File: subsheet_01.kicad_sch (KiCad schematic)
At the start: 0 parts

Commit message: Begins the CPU
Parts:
- added NT1: NetTie_2, symbol Device:NetTie_2
- added U1: MC68000_PLCC_68_PHY, Package_LCC:PLCC-68_THT-Socket, symbol mc_68000_plcc68:MC68000_PLCC_68_PHY
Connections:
- new net A1: U1.32 (A1)
- new net A10: U1.41 (A10)
- new net A11: U1.42 (A11)
- new net A12: U1.43 (A12)
- new net A13: U1.44 (A13)
- new net A14: U1.45 (A14)
- new net A15: U1.46 (A15)
- new net A16: U1.47 (A16)
- new net A17: U1.48 (A17)
- new net A18: U1.49 (A18)
- new net A19: U1.50 (A19)
- new net A2: U1.33 (A2)
- new net A20: U1.51 (A20)
- new net A21: U1.53 (A21)
- new net A22: U1.54 (A22)
- new net A23: U1.55 (A23)
- new net A3: U1.34 (A3)
- new net A4: U1.35 (A4)
- new net A5: U1.36 (A5)
- new net A6: U1.37 (A6)
- new net A7: U1.38 (A7)
- new net A8: U1.39 (A8)
- new net A9: U1.40 (A9)
- new net CPU_CLOCK: U1.15 (CLK)
- new net CPU_R/~{W}: U1.9 (R/~{W})
- new net D0: U1.5 (D0)
- new net D1: U1.4 (D1)
- new net D10: U1.63 (D10)
- new net D11: U1.62 (D11)
- new net D12: U1.61 (D12)
- new net D13: U1.60 (D13)
- new net D14: U1.59 (D14)
- new net D15: U1.58 (D15)
- new net D2: U1.3 (D2)
- new net D3: U1.2 (D3)
- new net D4: U1.1 (D4)
- new net D5: U1.68 (D5)
- new net D6: U1.67 (D6)
- new net D7: U1.66 (D7)
- new net D8: U1.65 (D8)
- new net D9: U1.64 (D9)
- new net FC0: U1.30 (FC0)
- new net FC1: U1.29 (FC1)
- new net FC2: U1.28 (FC2)
- new net IPL0: U1.27 (IPL0)
- new net IPL1: U1.26 (IPL1)
- new net IPL2: U1.25 (IPL2)
- new net ~{CPU_AS}: U1.6 (~{AS})
- new net ~{CPU_BGACK}: U1.12 (~{BGACK})
- new net ~{CPU_BG}: U1.11 (~{BG})
- new net ~{CPU_BR}: U1.13 (~{BR})
- new net ~{CPU_DTACK}: U1.10 (~{DTACK})
- new net ~{CPU_HALT}: U1.19 (~{HALT})
- new net ~{CPU_LDS}: U1.8 (~{LDS})
- new net ~{CPU_RESET}: U1.20 (~{RESET})
- new net ~{CPU_UDS}: U1.7 (~{UDS})
- no-connect marks 0 -> 3

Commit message: Continue CPU
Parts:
- added C1, C2: 0.22uF, symbol Device:C_Small
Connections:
- net 3V3_CPU: now reaches U1.14 (VCC)
- net 3V3_CPU: now also NT1.2, U1.52 (VCC), C1.1, C2.1
- net GND: now reaches U1.16 (GND)
- net GND: now also U1.17 (GND), U1.56 (GND), U1.57 (GND), C1.2, C2.2
- net +3V3: now reaches NT1.1
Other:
- note added: "TODO : * pull-up (give local labels to signals) * A0, A[24..31] and D[16..31] are left alone * ~{BERR} is missing !"
- moved on the sheet: NT1

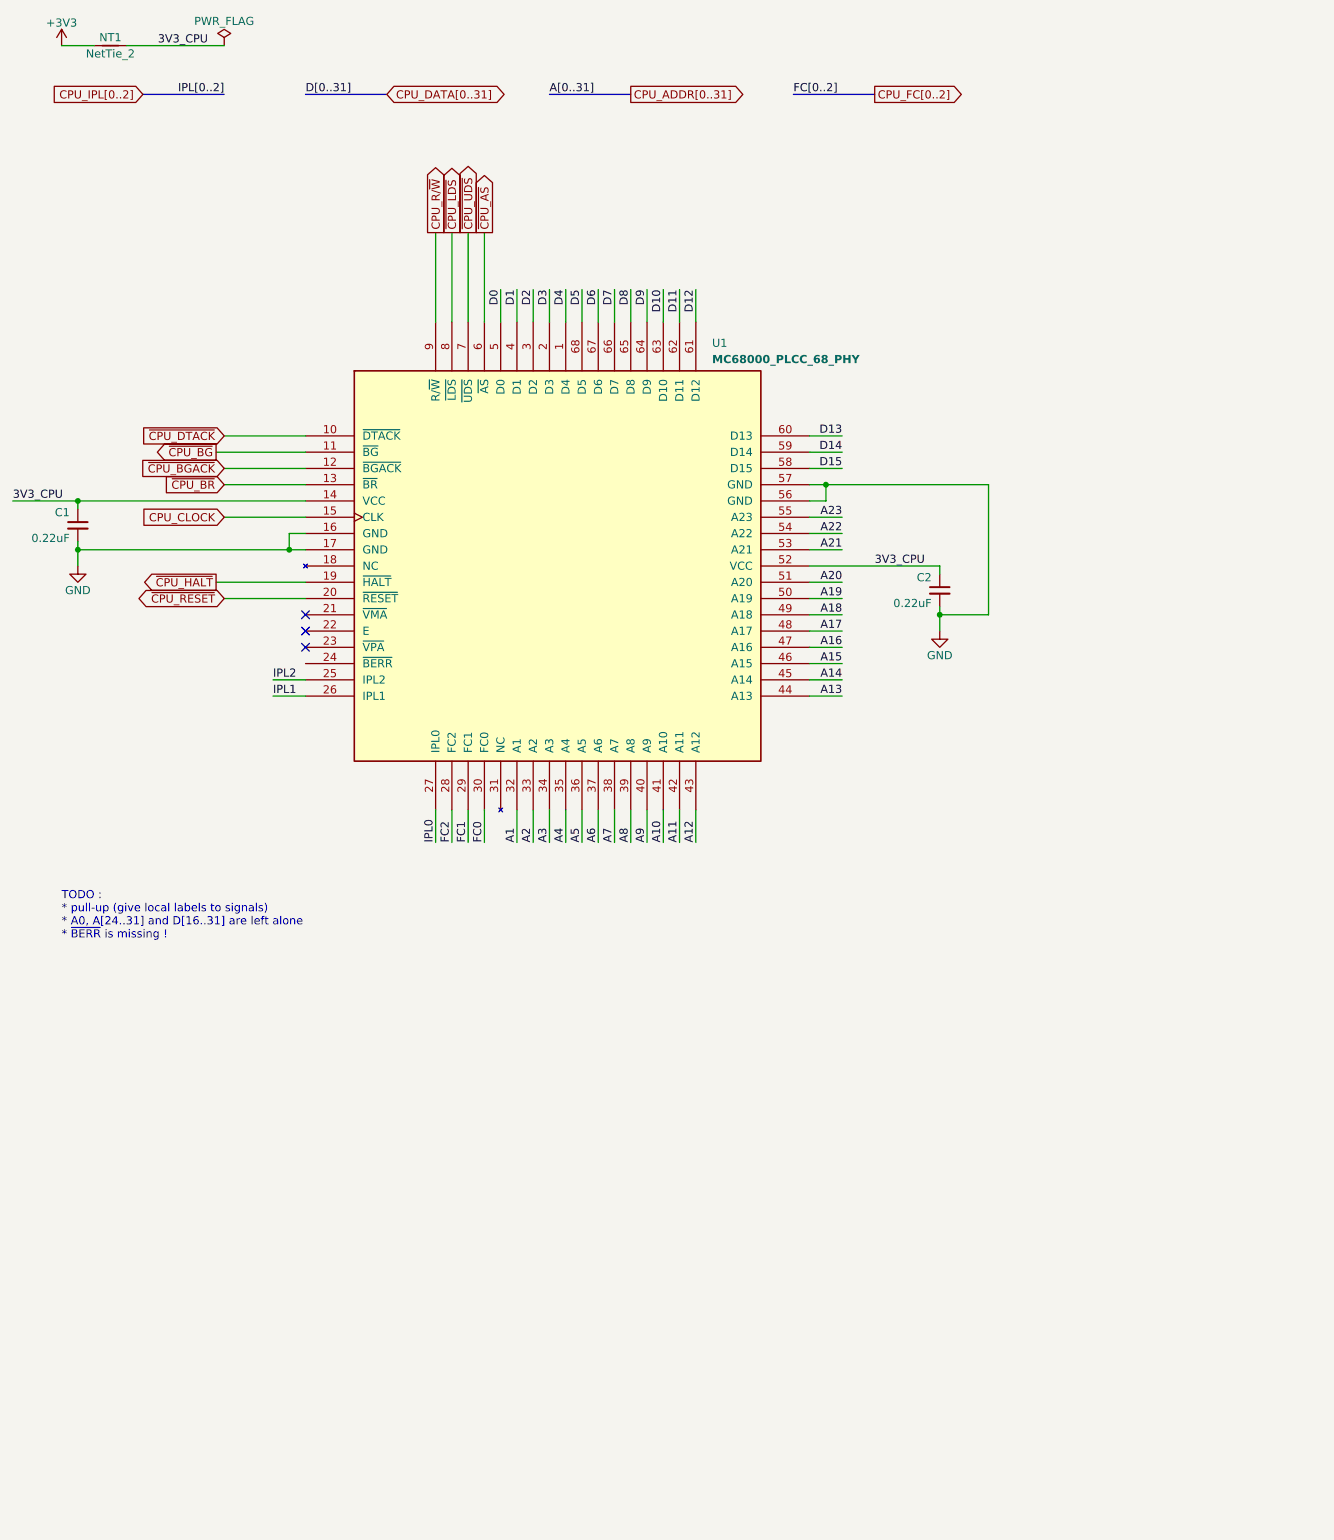
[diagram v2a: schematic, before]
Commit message: Completed CPU (for now), added notes to power supply sheet
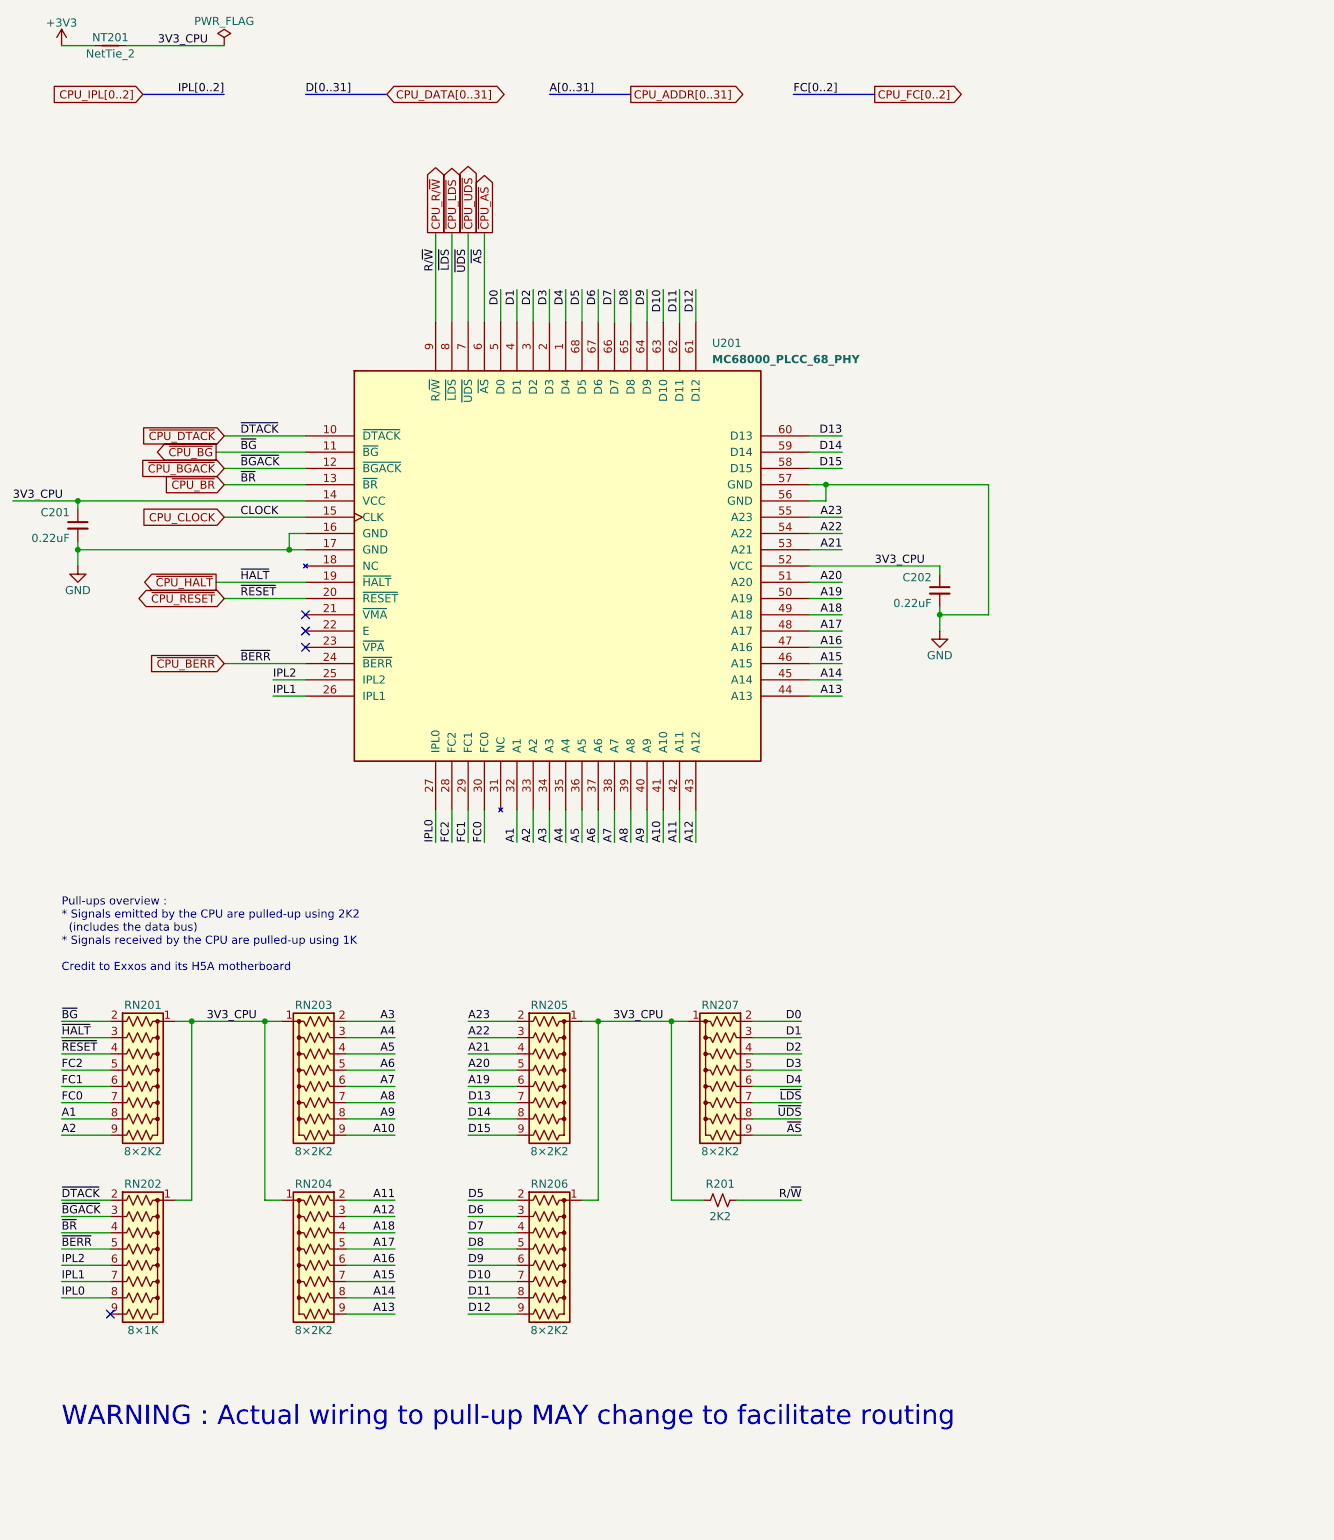
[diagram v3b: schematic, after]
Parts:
- added R201: 2K2, symbol Device:R_Small_US
- added RN201, RN203, RN204, RN205, RN206, RN207: 8×2K2, Resistor_THT:R_Array_SIP9, symbol Device:R_Network08_US
- added RN202: 8×1K, Resistor_THT:R_Array_SIP9, symbol Device:R_Network08_US
- renumbered C1 to C201, C2 to C202, NT1 to NT201, U1 to U201
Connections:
- net 3V3_CPU: now also R201.1, RN201.1 (common), RN202.1 (common), RN203.1 (common), RN204.1 (common), RN205.1 (common), RN206.1 (common), RN207.1 (common)
- net A1: now also RN201.8 (R7)
- net A10: now also RN203.9 (R8)
- net A11: now also RN204.2 (R1)
- net A12: now also RN204.3 (R2)
- net A13: now also RN204.9 (R8)
- net A14: now also RN204.8 (R7)
- net A15: now also RN204.7 (R6)
- net A16: now also RN204.6 (R5)
- net A17: now also RN204.5 (R4)
- net A18: now also RN204.4 (R3)
- net A19: now also RN205.6 (R5)
- net A2: now also RN201.9 (R8)
- net A20: now also RN205.5 (R4)
- net A21: now also RN205.4 (R3)
- net A22: now also RN205.3 (R2)
- net A23: now also RN205.2 (R1)
- net A3: now also RN203.2 (R1)
- net A4: now also RN203.3 (R2)
- net A5: now also RN203.4 (R3)
- net A6: now also RN203.5 (R4)
- net A7: now also RN203.6 (R5)
- net A8: now also RN203.7 (R6)
- net A9: now also RN203.8 (R7)
- net CPU_R/~{W}: now also R201.2
- net D0: now also RN207.2 (R1)
- net D1: now also RN207.3 (R2)
- net D10: now also RN206.7 (R6)
- net D11: now also RN206.8 (R7)
- net D12: now also RN206.9 (R8)
- net D13: now also RN205.7 (R6)
- net D14: now also RN205.8 (R7)
- net D15: now also RN205.9 (R8)
- net D2: now also RN207.4 (R3)
- net D3: now also RN207.5 (R4)
- net D4: now also RN207.6 (R5)
- net D5: now also RN206.2 (R1)
- net D6: now also RN206.3 (R2)
- net D7: now also RN206.4 (R3)
- net D8: now also RN206.5 (R4)
- net D9: now also RN206.6 (R5)
- net FC0: now also RN201.7 (R6)
- net FC1: now also RN201.6 (R5)
- net FC2: now also RN201.5 (R4)
- net IPL0: now also RN202.8 (R7)
- net IPL1: now also RN202.7 (R6)
- net IPL2: now also RN202.6 (R5)
- net ~{CPU_AS}: now also RN207.9 (R8)
- net ~{CPU_BGACK}: now also RN202.3 (R2)
- net ~{CPU_BG}: now also RN201.2 (R1)
- net ~{CPU_BR}: now also RN202.4 (R3)
- net ~{CPU_DTACK}: now also RN202.2 (R1)
- net ~{CPU_HALT}: now also RN201.3 (R2)
- net ~{CPU_LDS}: now also RN207.7 (R6)
- net ~{CPU_RESET}: now also RN201.4 (R3)
- net ~{CPU_UDS}: now also RN207.8 (R7)
- net ~{CPU_BERR}: now reaches U201.24 (~{BERR})
- net ~{CPU_BERR}: now also RN202.5 (R4)
- no-connect marks 3 -> 4
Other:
- note added: "Pull-ups overview : * Signals emitted by the CPU are pulled-up using 2K2 (includes the data bus) * Signals received by the CPU are pulled-up using 1K Credit to Exxos and its H5A motherboard"
- note added: "WARNING : Actual wiring to pull-up MAY change to facilitate routing"
- note removed: "TODO : * pull-up (give local labels to signals) * A0, A[24..31] and D[16..31] are left alone * ~{BERR} is missing !"

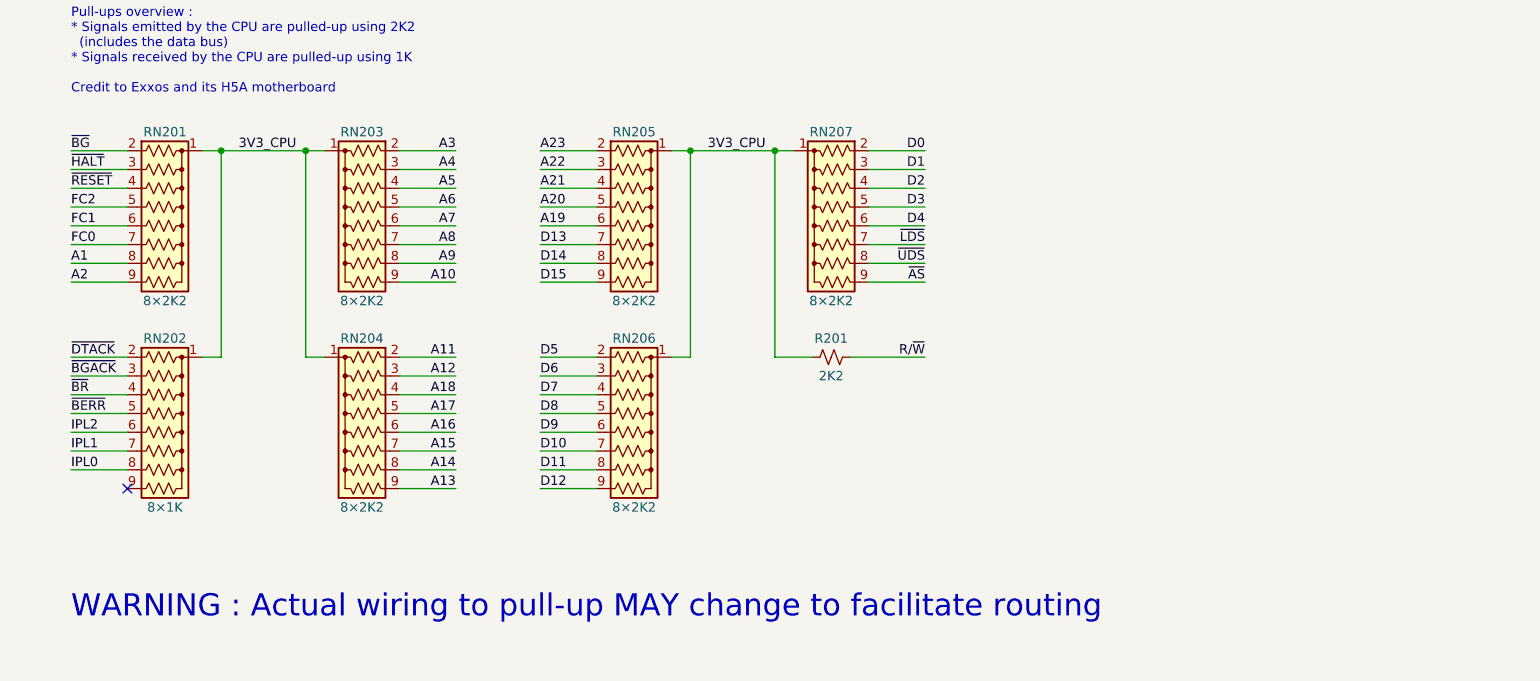
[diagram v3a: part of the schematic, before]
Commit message: CPU : pulled up addr24..addr31 ; CPLD : started
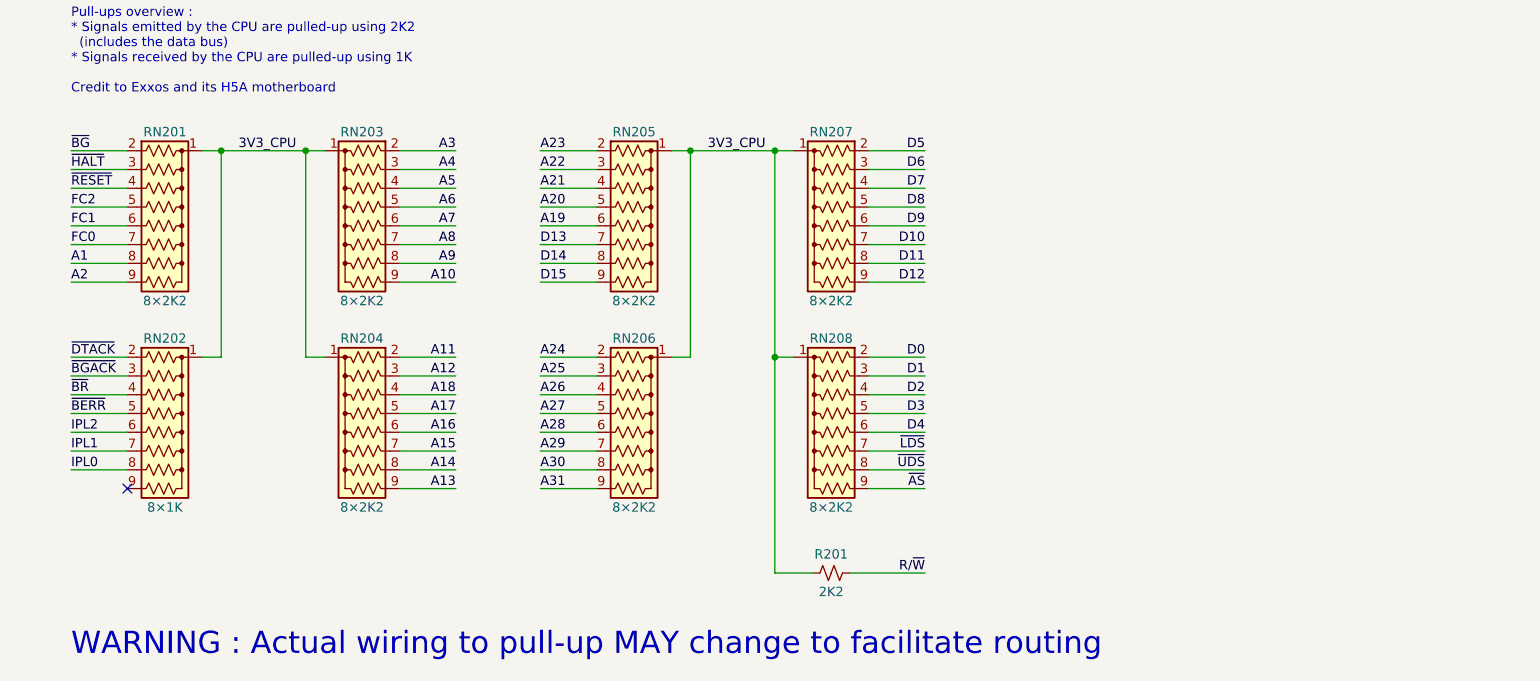
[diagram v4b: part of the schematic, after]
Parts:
- added RN208: 8×2K2, Resistor_THT:R_Array_SIP9, symbol Device:R_Network08_US
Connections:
- net 3V3_CPU: now also RN208.1 (common)
- net D0: now also RN208.2 (R1); no longer RN207.2 (R1)
- net D1: now also RN208.3 (R2); no longer RN207.3 (R2)
- net D10: now also RN207.7 (R6); no longer RN206.7 (R6)
- net D11: now also RN207.8 (R7); no longer RN206.8 (R7)
- net D12: now also RN207.9 (R8); no longer RN206.9 (R8)
- net D2: now also RN208.4 (R3); no longer RN207.4 (R3)
- net D3: now also RN208.5 (R4); no longer RN207.5 (R4)
- net D4: now also RN208.6 (R5); no longer RN207.6 (R5)
- net D5: now also RN207.2 (R1); no longer RN206.2 (R1)
- net D6: now also RN207.3 (R2); no longer RN206.3 (R2)
- net D7: now also RN207.4 (R3); no longer RN206.4 (R3)
- net D8: now also RN207.5 (R4); no longer RN206.5 (R4)
- net D9: now also RN207.6 (R5); no longer RN206.6 (R5)
- net ~{CPU_AS}: now also RN208.9 (R8); no longer RN207.9 (R8)
- net ~{CPU_LDS}: now also RN208.7 (R6); no longer RN207.7 (R6)
- net ~{CPU_UDS}: now also RN208.8 (R7); no longer RN207.8 (R7)
- new net A24: RN206.2 (R1)
- new net A25: RN206.3 (R2)
- new net A26: RN206.4 (R3)
- new net A27: RN206.5 (R4)
- new net A28: RN206.6 (R5)
- new net A29: RN206.7 (R6)
- new net A30: RN206.8 (R7)
- new net A31: RN206.9 (R8)
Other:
- moved on the sheet: R201
